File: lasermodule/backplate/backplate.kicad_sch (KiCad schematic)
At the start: 2 parts

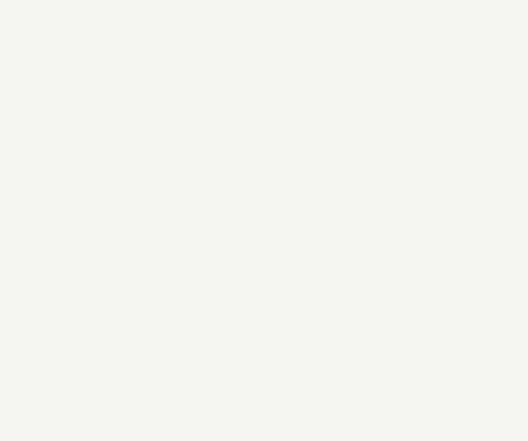
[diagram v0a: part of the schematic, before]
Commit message: removed need for screws using pcb pads
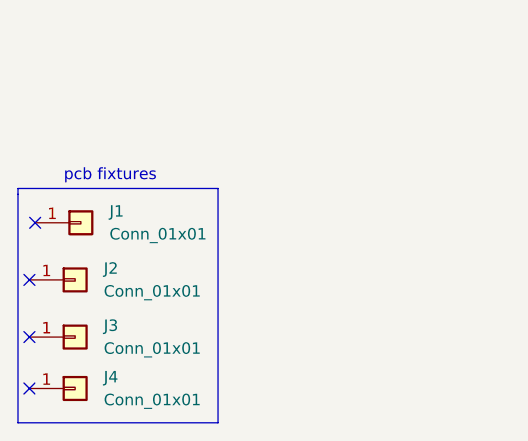
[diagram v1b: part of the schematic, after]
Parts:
- added J1, J2, J3, J4: Conn_01x01, footprints:TestPoint_Pad_2.0x2.0mm_nosilk, symbol Connector_Generic:Conn_01x01
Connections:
- no-connect marks 0 -> 4
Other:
- note added: "pcb fixtures"
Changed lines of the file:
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@@
 (kicad_sch (version 20230121) (generator eeschema)
   (paper "A4")
+  (no_connect (at 57.15 131.445))
+  (no_connect (at 57.15 137.795))
+  (no_connect (at 57.15 143.51))
+  (no_connect (at 57.785 125.095))
+  (polyline (pts (xy 55.88 147.32) (xy 78.105 147.32))
+    (stroke (width 0) (type default))
+  )
+  (polyline (pts (xy 78.105 121.285) (xy 55.88 121.285))
+    (stroke (width 0) (type default))
+  )
+  (polyline (pts (xy 55.88 121.285) (xy 55.88 121.92))
+    (stroke (width 0) (type default))
+  )
+  (polyline (pts (xy 78.105 147.32) (xy 78.105 121.285))
+    (stroke (width 0) (type default))
+  )
+  (polyline (pts (xy 55.88 121.92) (xy 55.88 147.32))
+    (stroke (width 0) (type default))
+  )
   (text "hexastorm front" (at 138.43 90.17 0)
+    (effects (font (size 1.27 1.27)) (justify left bottom))
+  )
+  (text "pcb fixtures" (at 60.96 120.65 0)
     (effects (font (size 1.27 1.27)) (justify left bottom))
   )
@@
         )
       )
+    )
+  )
+  (symbol (lib_id "Connector_Generic:Conn_01x01") (at 62.865 125.095 0) (unit 1)
+    (in_bom yes) (on_board yes) (dnp no) (fields_autoplaced)
+    (property "Reference" "J1" (at 66.04 123.825 0)
+      (effects (font (size 1.27 1.27)) (justify left))
+    )
+    (property "Value" "Conn_01x01" (at 66.04 126.365 0)
+      (effects (font (size 1.27 1.27)) (justify left))
+    )
+    (property "Footprint" "footprints:TestPoint_Pad_2.0x2.0mm_nosilk" (at 62.865 125.095 0)
+      (effects (font (size 1.27 1.27)) hide)
+    )
+    (property "Datasheet" "~" (at 62.865 125.095 0)
+      (effects (font (size 1.27 1.27)) hide)
+    )
+    (pin "1")
+    (instances
+      (project "backplate"
+        (path "/ce297ce2-f1fb-4090-bdc6-dffec6733818"
+          (reference "J1") (unit 1)
+        )
+      )
+    )
+  )
+  (symbol (lib_id "Connector_Generic:Conn_01x01") (at 62.23 131.445 0) (unit 1)
+    (in_bom yes) (on_board yes) (dnp no) (fields_autoplaced)
+    (property "Reference" "J2" (at 65.405 130.175 0)
+      (effects (font (size 1.27 1.27)) (justify left))
+    )
+    (property "Value" "Conn_01x01" (at 65.405 132.715 0)
+      (effects (font (size 1.27 1.27)) (justify left))
+    )
+    (property "Footprint" "footprints:TestPoint_Pad_2.0x2.0mm_nosilk" (at 62.23 131.445 0)
+      (effects (font (size 1.27 1.27)) hide)
+    )
+    (property "Datasheet" "~" (at 62.23 131.445 0)
+      (effects (font (size 1.27 1.27)) hide)
+    )
+    (pin "1")
+    (instances
+      (project "backplate"
+        (path "/ce297ce2-f1fb-4090-bdc6-dffec6733818"
+          (reference "J2") (unit 1)
+        )
+      )
+    )
+  )
+  (symbol (lib_id "Connector_Generic:Conn_01x01") (at 62.23 143.51 0) (unit 1)
+    (in_bom yes) (on_board yes) (dnp no) (fields_autoplaced)
+    (property "Reference" "J4" (at 65.405 142.24 0)
+      (effects (font (size 1.27 1.27)) (justify left))
+    )
+    (property "Value" "Conn_01x01" (at 65.405 144.78 0)
+      (effects (font (size 1.27 1.27)) (justify left))
+    )
+    (property "Footprint" "footprints:TestPoint_Pad_2.0x2.0mm_nosilk" (at 62.23 143.51 0)
+      (effects (font (size 1.27 1.27)) hide)
+    )
+    (property "Datasheet" "~" (at 62.23 143.51 0)
+      (effects (font (size 1.27 1.27)) hide)
+    )
+    (pin "1")
+    (instances
+      (project "backplate"
+        (path "/ce297ce2-f1fb-4090-bdc6-dffec6733818"
+          (reference "J4") (unit 1)
+        )
+      )
+    )
+  )
+  (symbol (lib_id "Connector_Generic:Conn_01x01") (at 62.23 137.795 0) (unit 1)
+    (in_bom yes) (on_board yes) (dnp no) (fields_autoplaced)
+    (property "Reference" "J3" (at 65.405 136.525 0)
+      (effects (font (size 1.27 1.27)) (justify left))
+    )
+    (property "Value" "Conn_01x01" (at 65.405 139.065 0)
+      (effects (font (size 1.27 1.27)) (justify left))
+    )
+    (property "Footprint" "footprints:TestPoint_Pad_2.0x2.0mm_nosilk" (at 62.23 137.795 0)
+      (effects (font (size 1.27 1.27)) hide)
+    )
+    (property "Datasheet" "~" (at 62.23 137.795 0)
+      (effects (font (size 1.27 1.27)) hide)
+    )
+    (pin "1")
+    (instances
+      (project "backplate"
+        (path "/ce297ce2-f1fb-4090-bdc6-dffec6733818"
+          (reference "J3") (unit 1)
+        )
+      )

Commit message: board almost fully synced close for release
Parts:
- removed L1, L2: Logo_Open_Hardware_Large, footprints:hexastorm, symbol Graphic:Logo_Open_Hardware_Large
- added J5: Conn_01x02, footprints:pogopincontact, symbol Connector_Generic:Conn_01x02
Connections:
- net +12V: now reaches J1.1 (Pin_1)
- net +12V: now also J5.2 (Pin_2)
- net LDK: now reaches J4.1 (Pin_1)
- net LDK: now also J5.1 (Pin_1)
- no-connect marks 4 -> 2
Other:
- note removed: "hexastorm front"
- note removed: "kicad back"
- moved on the sheet: J1, J2, J3, J4

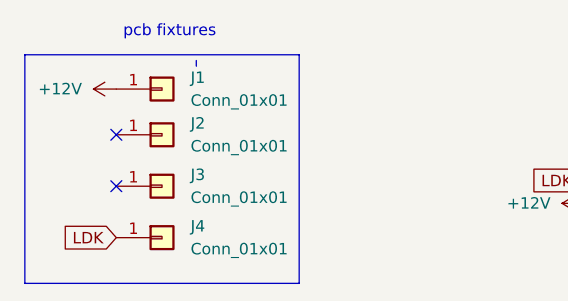
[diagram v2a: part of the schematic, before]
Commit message: added kicost tracking other plates, fixed plates
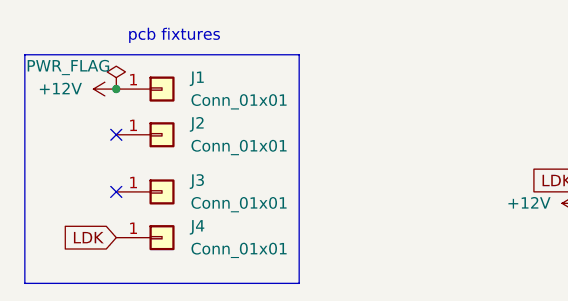
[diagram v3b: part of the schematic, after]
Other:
- moved on the sheet: J3
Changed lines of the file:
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@@
 	(generator_version "8.0")
 	(paper "A4")
+	(junction
+		(at 82.55 73.66)
+		(diameter 0)
+		(color 0 0 0 0)
+	)
 	(no_connect
-		(at 82.55 84.455)
+		(at 82.55 85.09)
 	)
 	(no_connect
@@
 	(polyline
 		(pts
-			(xy 91.44 70.485) (xy 91.44 71.12)
+			(xy 91.44 71.12) (xy 91.44 71.12)
 		)
 		(stroke
@@
 	(text "pcb fixtures"
 		(exclude_from_sim no)
-		(at 83.312 68.072 0)
+		(at 83.82 68.58 0)
 		(effects
 			(font
@@
 	(symbol
 		(lib_id "Connector_Generic:Conn_01x01")
-		(at 87.63 84.455 0)
+		(at 87.63 85.09 0)
 		(unit 1)
 		(exclude_from_sim no)
@@
 		(fields_autoplaced yes)
 		(property "Reference" "J3"
-			(at 90.805 83.185 0)
+			(at 90.805 83.82 0)
 			(effects
 				(font
@@
 		)
 		(property "Value" "Conn_01x01"
-			(at 90.805 85.725 0)
+			(at 90.805 86.36 0)
 			(effects
 				(font
@@
 		)
 		(property "Footprint" "footprints:TestPoint_Pad_2.0x2.0mm_nosilk"
-			(at 87.63 84.455 0)
+			(at 87.63 85.09 0)
 			(effects
 				(font
@@
 		)
 		(property "Datasheet" "~"
-			(at 87.63 84.455 0)
+			(at 87.63 85.09 0)
 			(effects
 				(font
@@
 		)
 		(property "Description" ""
-			(at 87.63 84.455 0)
+			(at 87.63 85.09 0)
 			(effects
 				(font
@@
 					(unit 1)
 				)
+			)
+		)
+	)
+	(symbol
+		(lib_id "power:PWR_FLAG")
+		(at 82.55 73.66 0)
+		(unit 1)
+		(exclude_from_sim no)
+		(in_bom yes)
+		(on_board yes)
+		(dnp no)
+		(property "Reference" "#FLG01"
+			(at 82.55 71.755 0)
+			(effects
+				(font
+					(size 1.27 1.27)
+				)
+				(hide yes)
+			)
+		)
+		(property "Value" "PWR_FLAG"
+			(at 77.216 71.12 0)
+			(effects
+				(font
+					(size 1.27 1.27)
+				)
+			)
+		)
+		(property "Footprint" ""
+			(at 82.55 73.66 0)
+			(effects
+				(font
+					(size 1.27 1.27)
+				)
+				(hide yes)
+			)
+		)
+		(property "Datasheet" "~"
+			(at 82.55 73.66 0)
+			(effects
+				(font
+					(size 1.27 1.27)
+				)
+				(hide yes)
+			)
+		)
+		(property "Description" "Special symbol for telling ERC where power comes from"
+			(at 82.55 73.66 0)
+			(effects
+				(font
+					(size 1.27 1.27)
+				)
+				(hide yes)
+			)
+		)
+		(pin "1"
+		)
+		(instances
+			(project ""
+				(path "/ce297ce2-f1fb-4090-bdc6-dffec6733818"
+					(reference "#FLG01")
+					(unit 1)
+				)
